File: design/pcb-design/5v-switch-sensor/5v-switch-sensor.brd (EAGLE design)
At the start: 41.6 x 43.2 mm, 24 parts

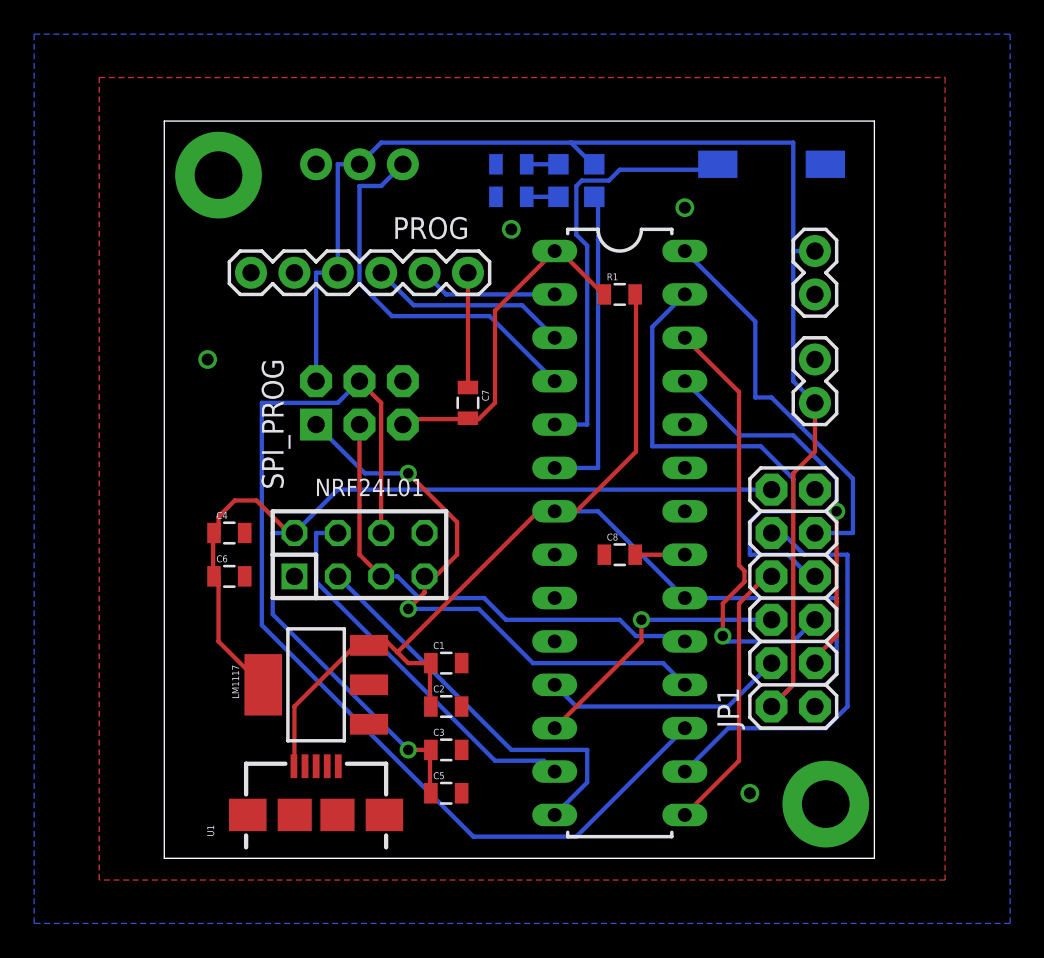
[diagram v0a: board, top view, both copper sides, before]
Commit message: pcb-design: [5v-switch-sensor] added noise reduction to IR circuit
Signed-off-by: Kiveisha Yevgeniy <lodmilak@gmail.com>
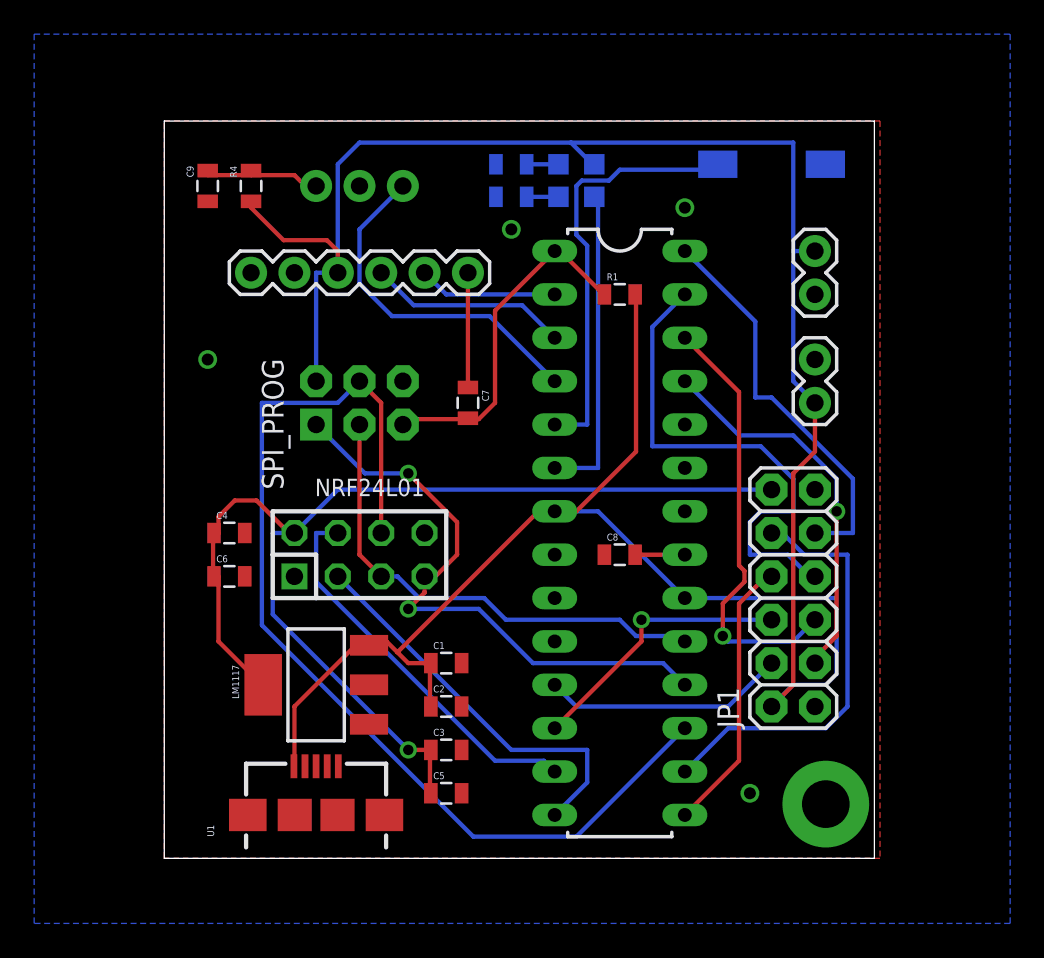
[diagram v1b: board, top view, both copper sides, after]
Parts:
- added C9: 2.2u, SparkFun-Capacitors:0805
- added R4: 220, SparkFun-Resistors:0805
- moved IR 1.27 mm to (31.8, 38.1)
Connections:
- new net N$1: C9.2, IR.3, R4.2
- net 5V: now also R4.1; no longer IR.2
- net GND: now also C9.1, IR.2; no longer IR.3
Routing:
- net 5V: track 150.9 -> 158.7 mm
- net N$1: track 0.00 -> 7.14 mm
- net D2: track 22.6 -> 20.6 mm
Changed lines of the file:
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@@
 <?xml version="1.0" encoding="utf-8"?>
 <!DOCTYPE eagle SYSTEM "eagle.dtd">
-<eagle version="7.1.0">
+<eagle version="7.2.0">
 <drawing>
 <settings>
@@
 <wire x1="59.36" y1="41.9" x2="17.78" y2="41.9" width="0" layer="20"/>
 <wire x1="17.78" y1="41.9" x2="17.78" y2="-1.27" width="0" layer="20"/>
+<dimension x1="17.78" y1="-1.27" x2="17.78" y2="41.91" x3="15.24" y3="20.32" textsize="1.778" layer="1"/>
+<dimension x1="17.78" y1="41.91" x2="59.69" y2="41.91" x3="38.735" y3="44.45" textsize="1.778" layer="1"/>
 </plain>
 <attributes>
@@
 <description language="de">&lt;b&gt;EAGLE Design Rules&lt;/b&gt;
 &lt;p&gt;
-Die Standard-Design-Rules sind so gewÃÂÃÂ¤hlt, dass sie fÃÂÃÂ¼r
+Die Standard-Design-Rules sind so gewÃÂÃÂÃÂÃÂ¤hlt, dass sie fÃÂÃÂÃÂÃÂ¼r
 die meisten Anwendungen passen. Sollte ihre Platine
 besondere Anforderungen haben, treffen Sie die erforderlichen
@@
 <param name="TopRouterVariant" value="1"/>
 <param name="tpViaShape" value="round"/>
-<param name="PrefDir.1" value="*"/>
+<param name="PrefDir.1" value="a"/>
 <param name="PrefDir.2" value="0"/>
 <param name="PrefDir.3" value="0"/>
@@
 <param name="PrefDir.14" value="0"/>
 <param name="PrefDir.15" value="0"/>
-<param name="PrefDir.16" value="-"/>
+<param name="PrefDir.16" value="a"/>
 <param name="cfVia" value="8"/>
 <param name="cfNonPref" value="5"/>
@@
 <element name="C7" library="SparkFun-Capacitors" package="0805" value="0.1u" x="35.56" y="25.4" rot="R270"/>
 <element name="C8" library="SparkFun-Capacitors" package="0805" value="0.1u" x="44.45" y="16.51"/>
-<element name="IR" library="SparkFun-Connectors" package="1X03" value="" x="31.75" y="39.37" smashed="yes" rot="MR0">
-<attribute name="NAME" x="26.7462" y="36.1188" size="1.27" layer="26" ratio="10" rot="MR0"/>
-<attribute name="VALUE" x="33.02" y="36.195" size="1.27" layer="28" rot="MR0"/>
+<element name="IR" library="SparkFun-Connectors" package="1X03" value="" x="31.75" y="38.1" smashed="yes" rot="MR0">
+<attribute name="VALUE" x="33.02" y="34.925" size="1.27" layer="28" rot="MR0"/>
 </element>
 <element name="LM1117" library="SparkFun-PowerIC" package="SOT223" value="" x="26.67" y="8.89" rot="R90">
@@
 </element>
 <element name="PROG" library="SparkFun-Connectors" package="1X06" value="" x="35.56" y="33.02" smashed="yes" rot="R180">
-<attribute name="NAME" x="35.6362" y="36.2712" size="1.27" layer="25" ratio="10" rot="R180"/>
 <attribute name="VALUE" x="36.83" y="36.195" size="1.27" layer="27" rot="R180"/>
 </element>
@@
 <attribute name="PROD_ID" value="CONN-12423" x="55.88" y="7.62" size="1.778" layer="27" rot="R90" display="off"/>
 <attribute name="NAME" x="51.435" y="6.35" size="1.27" layer="25" ratio="10" rot="R90"/>
+</element>
+<element name="R4" library="SparkFun-Resistors" package="0805" value="220" x="22.86" y="38.1" smashed="yes" rot="R90">
+<attribute name="NAME" x="22.0345" y="38.608" size="0.4064" layer="25" rot="R90"/>
+<attribute name="VALUE" x="21.463" y="37.846" size="0.4064" layer="27" rot="R270"/>
+</element>
+<element name="C9" library="SparkFun-Capacitors" package="0805" value="2.2u" x="20.32" y="38.1" smashed="yes" rot="R90">
+<attribute name="NAME" x="19.4945" y="38.608" size="0.4064" layer="25" rot="R90"/>
+<attribute name="VALUE" x="18.923" y="37.846" size="0.4064" layer="27" rot="R270"/>
 </element>
 </elements>
@@
 <contactref element="ATMEGA" pad="22"/>
 <contactref element="ATMEGA" pad="8"/>
-<contactref element="IR" pad="3"/>
 <contactref element="5V-F" pad="1"/>
 <contactref element="5V-R" pad="1"/>
@@
 </polygon>
 <polygon width="0.4064" layer="1">
-<vertex x="13.97" y="44.45"/>
-<vertex x="63.5" y="44.45"/>
-<vertex x="63.5" y="-2.54"/>
-<vertex x="13.97" y="-2.54"/>
+<vertex x="17.78" y="41.91"/>
+<vertex x="59.69" y="41.91"/>
+<vertex x="59.69" y="-1.27"/>
+<vertex x="17.78" y="-1.27"/>
 </polygon>
 <contactref element="R2" pad="1"/>
@@
 <via x="20.32" y="27.94" extent="1-16" drill="0.7"/>
 <via x="52.07" y="2.54" extent="1-16" drill="0.7"/>
+<contactref element="C9" pad="1"/>
+<contactref element="IR" pad="2"/>
 </signal>
 <signal name="5V">
@@
 <contactref element="PROG" pad="4"/>
 <contactref element="R1" pad="2"/>
-<contactref element="IR" pad="2"/>
 <contactref element="5V-F" pad="2"/>
 <contactref element="5V-R" pad="2"/>
@@
 <wire x1="27.94" y1="33.02" x2="26.67" y2="33.02" width="0.254" layer="16"/>
 <wire x1="41.5925" y1="40.64" x2="42.8625" y2="39.37" width="0.254" layer="16"/>
-<wire x1="30.48" y1="40.64" x2="41.5925" y2="40.64" width="0.254" layer="16"/>
-<wire x1="29.21" y1="39.37" x2="30.48" y2="40.64" width="0.254" layer="16"/>
+<wire x1="29.21" y1="40.64" x2="41.5925" y2="40.64" width="0.254" layer="16"/>
 <wire x1="42.8625" y1="39.37" x2="42.96" y2="39.37" width="0.254" layer="16"/>
 <wire x1="27.94" y1="39.37" x2="27.94" y2="33.02" width="0.254" layer="16"/>
-<wire x1="29.21" y1="39.37" x2="27.94" y2="39.37" width="0.254" layer="16"/>
 <wire x1="54.61" y1="40.64" x2="54.61" y2="34.29" width="0.254" layer="16"/>
 <wire x1="41.5925" y1="40.64" x2="54.61" y2="40.64" width="0.254" layer="16"/>
@@
 <wire x1="54.61" y1="8.89" x2="54.61" y2="21.2725" width="0.254" layer="1"/>
 <wire x1="53.34" y1="7.62" x2="54.61" y2="8.89" width="0.254" layer="1"/>
+<contactref element="R4" pad="1"/>
+<wire x1="24.765" y1="34.925" x2="22.86" y2="36.83" width="0.254" layer="1"/>
+<wire x1="27.305" y1="34.925" x2="24.765" y2="34.925" width="0.254" layer="1"/>
+<wire x1="27.94" y1="34.29" x2="27.305" y2="34.925" width="0.254" layer="1"/>
+<wire x1="27.94" y1="33.02" x2="27.94" y2="34.29" width="0.254" layer="1"/>
+<wire x1="22.86" y1="36.83" x2="22.86" y2="37.2" width="0.254" layer="1"/>
+<wire x1="29.21" y1="40.64" x2="27.94" y2="39.37" width="0.254" layer="16"/>
 </signal>
 <signal name="SCK">
@@
 <wire x1="31.115" y1="30.48" x2="36.83" y2="30.48" width="0.254" layer="16"/>
 <wire x1="29.21" y1="32.385" x2="31.115" y2="30.48" width="0.254" layer="16"/>
-<wire x1="29.21" y1="38.1" x2="29.21" y2="32.385" width="0.254" layer="16"/>
-<wire x1="30.48" y1="38.1" x2="29.21" y2="38.1" width="0.254" layer="16"/>
-<wire x1="31.75" y1="39.37" x2="30.48" y2="38.1" width="0.254" layer="16"/>
+<wire x1="29.21" y1="35.56" x2="29.21" y2="32.385" width="0.254" layer="16"/>
+<wire x1="31.75" y1="38.1" x2="29.21" y2="35.56" width="0.254" layer="16"/>
 </signal>
 <signal name="D3-PWM">
@@
 <signal name="N$6">
 <via x="56.515" y="1.905" extent="1-16" drill="2.794" diameter="5.08"/>
-</signal>
-<signal name="N$5">
-<via x="20.955" y="38.735" extent="1-16" drill="2.794" diameter="5.08"/>
 </signal>
 <signal name="3V3">
@@
 <via x="32.0675" y="5.08" extent="1-16" drill="0.6096"/>
 </signal>
+<signal name="N$1">
+<contactref element="R4" pad="2"/>
+<contactref element="C9" pad="2"/>
+<contactref element="IR" pad="3"/>
+<wire x1="22.86" y1="38.735" x2="20.32" y2="38.735" width="0.254" layer="1"/>
+<wire x1="20.32" y1="38.735" x2="20.32" y2="39" width="0.254" layer="1"/>
+<wire x1="25.4" y1="38.735" x2="22.86" y2="38.735" width="0.254" layer="1"/>
+<wire x1="26.035" y1="38.1" x2="25.4" y2="38.735" width="0.254" layer="1"/>
+<wire x1="26.67" y1="38.1" x2="26.035" y2="38.1" width="0.254" layer="1"/>
+<wire x1="22.86" y1="38.735" x2="22.86" y2="39" width="0.254" layer="1"/>
+</signal>
 </signals>

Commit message: pcb-design: 5v pcb fixes before sendinf to imall and start of 3v pcb
Signed-off-by: Kiveisha Yevgeniy <lodmilak@gmail.com>
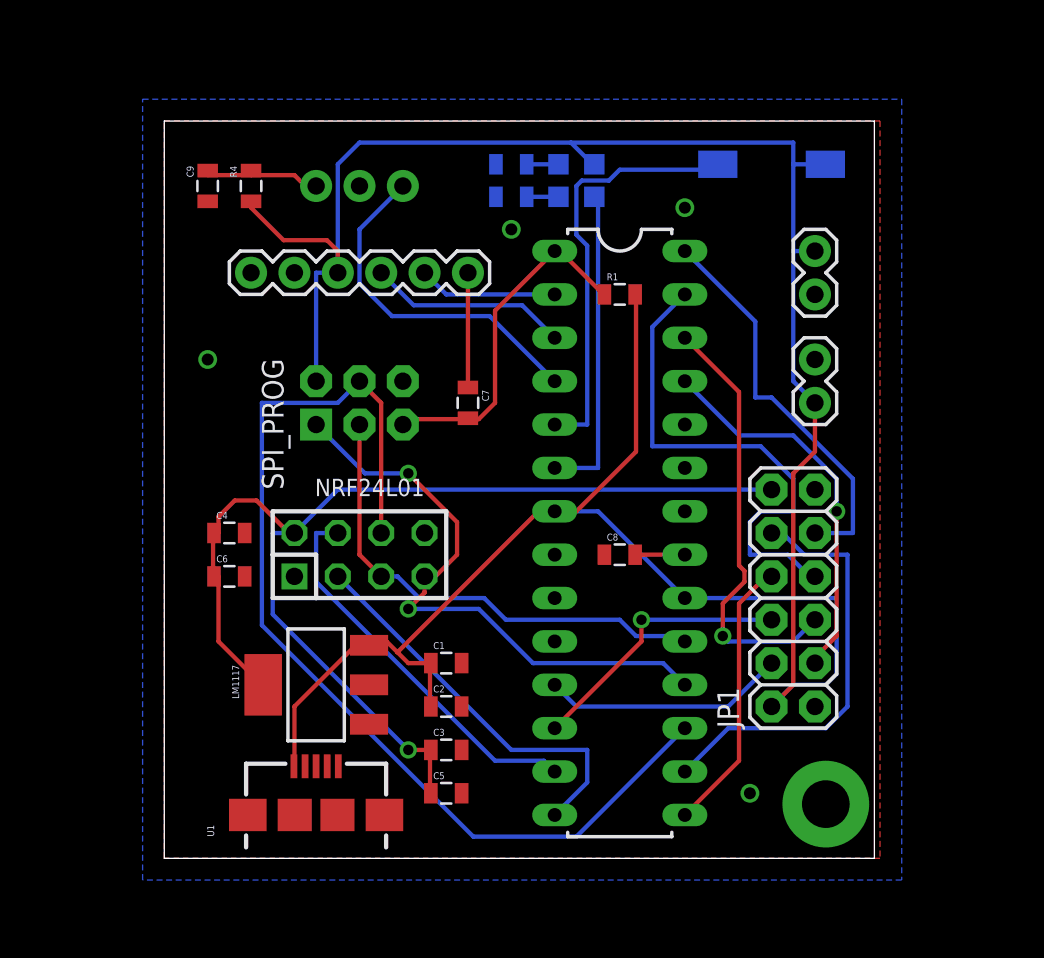
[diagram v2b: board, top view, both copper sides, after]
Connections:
- net 5V: now also S1.1
- net GND: no longer S1.1
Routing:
- net 5V: track 158.7 -> 160.6 mm
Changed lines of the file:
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@@
 <wire x1="59.36" y1="41.9" x2="17.78" y2="41.9" width="0" layer="20"/>
 <wire x1="17.78" y1="41.9" x2="17.78" y2="-1.27" width="0" layer="20"/>
-<dimension x1="17.78" y1="-1.27" x2="17.78" y2="41.91" x3="15.24" y3="20.32" textsize="1.778" layer="1"/>
-<dimension x1="17.78" y1="41.91" x2="59.69" y2="41.91" x3="38.735" y3="44.45" textsize="1.778" layer="1"/>
 </plain>
 <attributes>
@@
 <contactref element="SPI_PROG" pad="6"/>
 <polygon width="0.4064" layer="16">
-<vertex x="10.16" y="46.99"/>
-<vertex x="67.31" y="46.99"/>
-<vertex x="67.31" y="-5.08"/>
-<vertex x="10.16" y="-5.08"/>
+<vertex x="16.51" y="43.18"/>
+<vertex x="60.96" y="43.18"/>
+<vertex x="60.96" y="-2.54"/>
+<vertex x="16.51" y="-2.54"/>
 </polygon>
 <polygon width="0.4064" layer="1">
@@
 <contactref element="R2" pad="1"/>
 <contactref element="R3" pad="1"/>
-<contactref element="S1" pad="1"/>
 <contactref element="C5" pad="2"/>
 <contactref element="C3" pad="2"/>
@@
 <wire x1="42.8625" y1="39.37" x2="42.96" y2="39.37" width="0.254" layer="16"/>
 <wire x1="27.94" y1="39.37" x2="27.94" y2="33.02" width="0.254" layer="16"/>
-<wire x1="54.61" y1="40.64" x2="54.61" y2="34.29" width="0.254" layer="16"/>
+<wire x1="54.61" y1="40.64" x2="54.61" y2="39.37" width="0.254" layer="16"/>
+<wire x1="54.61" y1="39.37" x2="54.61" y2="34.29" width="0.254" layer="16"/>
 <wire x1="41.5925" y1="40.64" x2="54.61" y2="40.64" width="0.254" layer="16"/>
 <wire x1="33.3375" y1="10.16" x2="33.3375" y2="7.62" width="0.254" layer="1"/>
@@
 <wire x1="22.86" y1="36.83" x2="22.86" y2="37.2" width="0.254" layer="1"/>
 <wire x1="29.21" y1="40.64" x2="27.94" y2="39.37" width="0.254" layer="16"/>
+<contactref element="S1" pad="1"/>
+<wire x1="54.61" y1="39.37" x2="56.49" y2="39.37" width="0.254" layer="16"/>
 </signal>
 <signal name="SCK">
